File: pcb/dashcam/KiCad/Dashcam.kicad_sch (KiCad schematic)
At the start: 28 parts, among them J3 Conn_02x03_Odd_Even, J4 Conn_01x08_Pin, SW1 SW_Push, U1 WS2812B, U2 BC547, U3 ATTINY85-20SU, U4 WS2812B

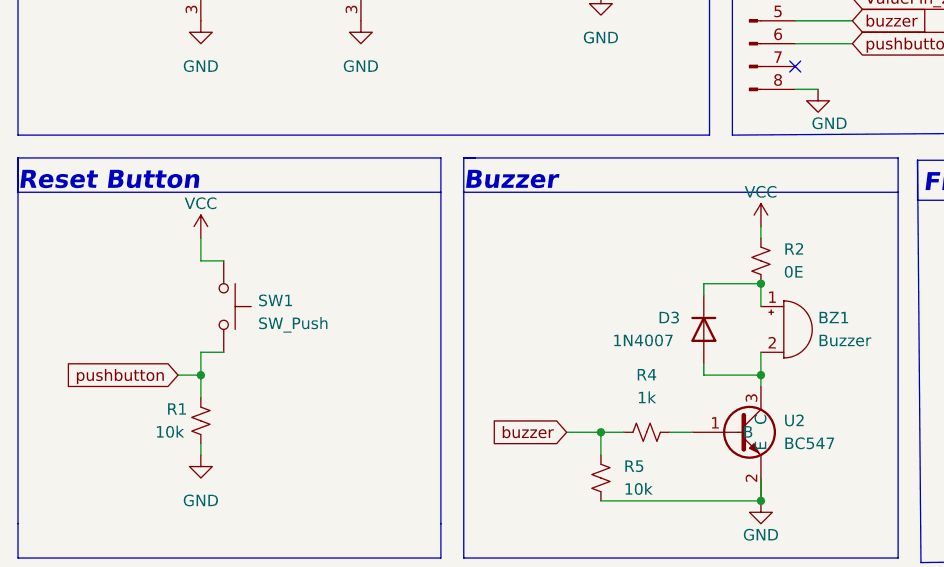
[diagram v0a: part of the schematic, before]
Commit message: diode removed added cap to push reset ckt
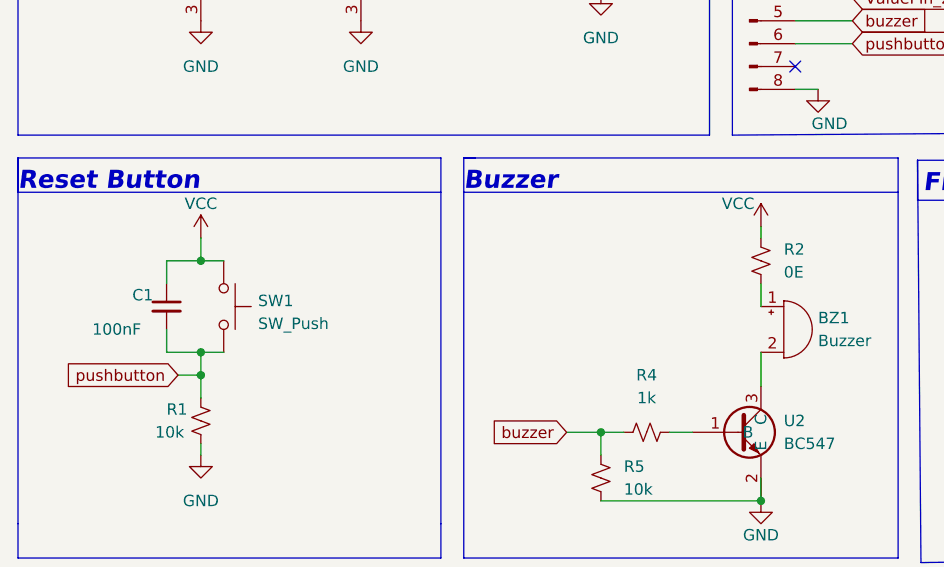
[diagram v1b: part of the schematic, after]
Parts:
- removed D3: 1N4007, Diode_SMD:D_SMA, symbol Diode:1N4007
- added C1: 100nF, Capacitor_SMD:C_0603_1608Metric, symbol Device:C_Small
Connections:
- net +5V: now also C1.1
- net pushbutton: now also C1.2
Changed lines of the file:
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@@
   (junction (at 92.964 134.366) (diameter 0) (color 0 0 0 0)
   )
-  (junction (at 97.79 71.12) (diameter 0) (color 0 0 0 0)
-  )
   (junction (at 86.614 161.036) (diameter 0) (color 0 0 0 0)
   )
@@
   (junction (at 49.784 134.366) (diameter 0) (color 0 0 0 0)
   )
-  (junction (at 97.79 81.28) (diameter 0) (color 0 0 0 0)
-  )
   (junction (at 80.01 87.63) (diameter 0) (color 0 0 0 0)
   )
   (junction (at 91.948 117.856) (diameter 0) (color 0 0 0 0)
   )
+  (junction (at 35.56 68.58) (diameter 0) (color 0 0 0 0)
+  )
   (junction (at 74.295 33.655) (diameter 0) (color 0 0 0 0)
   )
@@
   )
   (junction (at 45.974 139.446) (diameter 0) (color 0 0 0 0)
+  )
+  (junction (at 35.56 78.74) (diameter 0) (color 0 0 0 0)
   )
   (junction (at 90.424 157.226) (diameter 0) (color 0 0 0 0)
@@
     (stroke (width 0) (type default))
   )
+  (wire (pts (xy 31.75 78.74) (xy 35.56 78.74))
+    (stroke (width 0) (type default))
+  )
   (polyline (pts (xy 115.57 102.108) (xy 152.146 101.6))
     (stroke (width 0) (type default))
@@
     (stroke (width 0) (type default))
   )
+  (wire (pts (xy 31.75 71.12) (xy 31.75 68.58))
+    (stroke (width 0) (type default))
+  )
   (polyline (pts (xy 15.24 97.79) (xy 15.24 101.6))
     (stroke (width 0) (type default))
@@
     (stroke (width 0) (type default))
   )
-  (wire (pts (xy 91.44 72.39) (xy 91.44 71.12))
-    (stroke (width 0) (type default))
-  )
   (wire (pts (xy 76.2 87.63) (xy 80.01 87.63))
     (stroke (width 0) (type default))
@@
     (stroke (width 0) (type default))
   )
+  (wire (pts (xy 31.75 76.2) (xy 31.75 78.74))
+    (stroke (width 0) (type default))
+  )
   (wire (pts (xy 38.1 78.74) (xy 35.56 78.74))
     (stroke (width 0) (type default))
@@
     (stroke (width 0) (type default))
   )
-  (wire (pts (xy 91.44 80.01) (xy 91.44 81.28))
-    (stroke (width 0) (type default))
-  )
   (polyline (pts (xy 94.615 15.24) (xy 94.615 15.875))
     (stroke (width 0) (type default))
@@
     (stroke (width 0) (type default))
   )
-  (wire (pts (xy 97.79 81.28) (xy 97.79 82.55))
-    (stroke (width 0) (type default))
-  )
   (polyline (pts (xy 94.615 54.61) (xy 94.615 15.24))
     (stroke (width 0) (type default))
@@
     (stroke (width 0) (type default))
   )
-  (wire (pts (xy 91.44 71.12) (xy 97.79 71.12))
-    (stroke (width 0) (type default))
-  )
-  (wire (pts (xy 97.79 78.74) (xy 97.79 81.28))
+  (wire (pts (xy 97.79 78.74) (xy 97.79 82.55))
     (stroke (width 0) (type default))
   )
@@
     (stroke (width 0) (type default))
   )
-  (wire (pts (xy 91.44 81.28) (xy 97.79 81.28))
-    (stroke (width 0) (type default))
-  )
   (wire (pts (xy 35.56 68.58) (xy 38.1 68.58))
     (stroke (width 0) (type default))
   )
   (wire (pts (xy 80.01 87.63) (xy 80.01 90.17))
+    (stroke (width 0) (type default))
+  )
+  (wire (pts (xy 31.75 68.58) (xy 35.56 68.58))
     (stroke (width 0) (type default))
   )
@@
         (path "/e63e39d7-6ac0-4ffd-8aa3-1841a4541b55"
           (reference "U2") (unit 1)
-        )
-      )
-    )
-  )
-  (symbol (lib_id "Diode:1N4007") (at 91.44 76.2 270) (unit 1)
-    (in_bom yes) (on_board yes) (dnp no)
-    (property "Reference" "D3" (at 86.36 74.93 90)
-      (effects (font (size 1.27 1.27)) (justify left))
-    )
-    (property "Value" "1N4007" (at 81.28 77.47 90)
-      (effects (font (size 1.27 1.27)) (justify left))
-    )
-    (property "Footprint" "Diode_SMD:D_SMA" (at 86.995 76.2 0)
-      (effects (font (size 1.27 1.27)) hide)
-    )
-    (property "Datasheet" "http://www.vishay.com/docs/88503/1n4001.pdf" (at 91.44 76.2 0)
-      (effects (font (size 1.27 1.27)) hide)
-    )
-    (pin "1")
-    (pin "2")
-    (instances
-      (project "Dashcam"
-        (path "/e63e39d7-6ac0-4ffd-8aa3-1841a4541b55"
-          (reference "D3") (unit 1)
         )
       )
@@
       (effects (font (size 1.27 1.27)) hide)
     )
-    (property "Value" "VCC" (at 97.79 60.96 0)
+    (property "Value" "VCC" (at 95.25 62.23 0)
       (effects (font (size 1.27 1.27)))
     )
@@
         )
       )
+    )
+  )
+  (symbol (lib_id "Device:C_Small") (at 31.75 73.66 0) (unit 1)
+    (in_bom yes) (on_board yes) (dnp no)
+    (property "Reference" "C1" (at 27.94 72.39 0)
+      (effects (font (size 1.27 1.27)) (justify left))
+    )
+    (property "Value" "100nF" (at 23.495 76.2 0)
+      (effects (font (size 1.27 1.27)) (justify left))
+    )
+    (property "Footprint" "Capacitor_SMD:C_0603_1608Metric" (at 31.75 73.66 0)
+      (effects (font (size 1.27 1.27)) hide)
+    )
+    (property "Datasheet" "~" (at 31.75 73.66 0)
+      (effects (font (size 1.27 1.27)) hide)
+    )
+    (pin "1")
+    (pin "2")
+    (instances
+      (project "Dashcam"
+        (path "/e63e39d7-6ac0-4ffd-8aa3-1841a4541b55"
+          (reference "C1") (unit 1)
+        )
+      )

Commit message: pcb- pulldown removed, 470 ohm added in series
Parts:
- R7, R8, R9: value 10k -> 470R
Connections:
- net GND: no longer R7.1, R8.1, R9.1
- net LED Selector: now also R7.1; no longer J3.3 (Pin_3), R7.2, U3.7 (PB2)
- net ValuePin_1: now also R8.2; no longer R9.2, U3.2 (PB3)
- net ValuePin_2: now also R9.2; no longer R8.2, U3.3 (PB4)
- new net: R8.1, U3.2 (PB3)
- new net: R9.1, U3.3 (PB4)
- new net SEK: J3.3 (Pin_3), R7.2, U3.7 (PB2)
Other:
- moved on the sheet: BZ1, C1, C5, C6, C7, C8, DC_U1, DC_U4, FID1, FID2, FID3, FID4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
